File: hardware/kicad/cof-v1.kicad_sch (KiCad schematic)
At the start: 0 parts

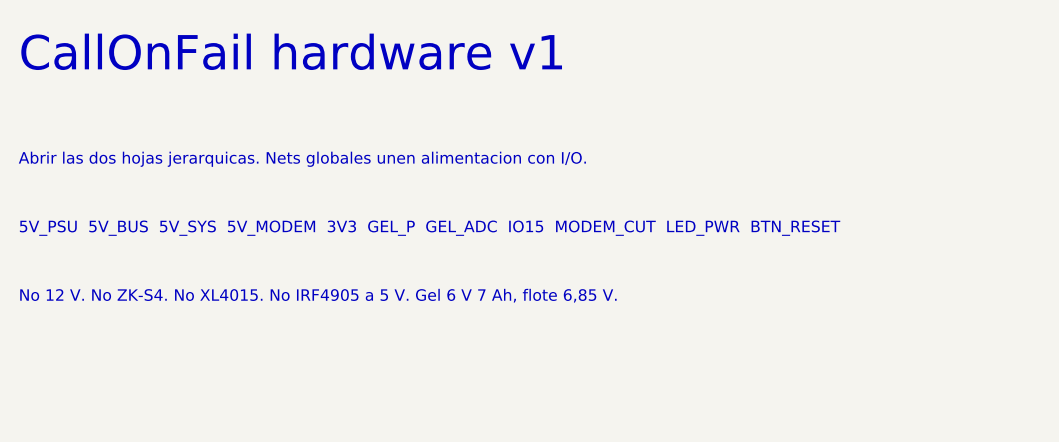
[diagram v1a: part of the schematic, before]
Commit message: Stop tracking PDFs and generated KiCad dumps; set WiFi from the web over Ethernet.
Vendor manuals, schematic PDFs, SVG previews and ERC reports do not belong in git or agent context. Firmware prefers Ethernet and accepts set_wifi/clear_wifi from the device page.

Co-authored-by: Cursor <cursoragent@cursor.com>
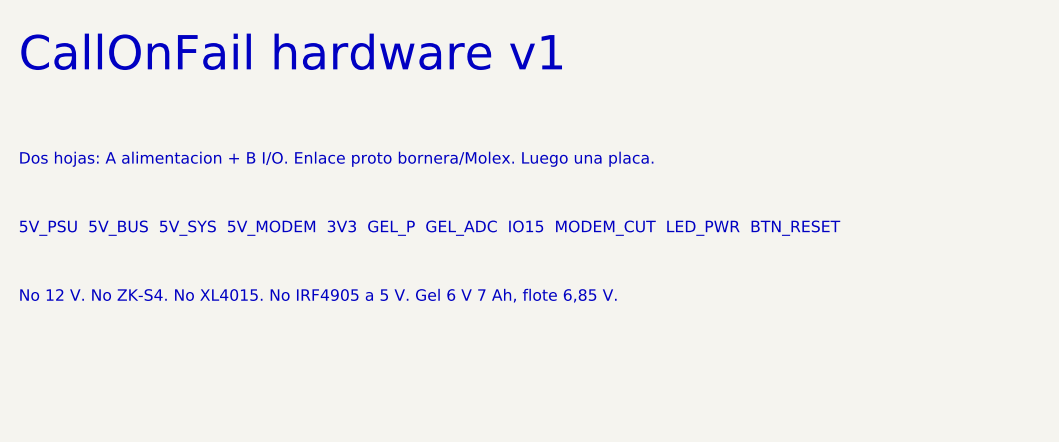
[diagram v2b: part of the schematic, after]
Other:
- note added: "Dos hojas: A alimentacion + B I/O. Enlace proto bornera/Molex. Luego una placa."
- note removed: "Abrir las dos hojas jerarquicas. Nets globales unen alimentacion con I/O."
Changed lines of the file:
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@@
 (kicad_sch
-	(version 20241209)
+	(version 20260306)
 	(generator "eeschema")
 	(generator_version "10.0")
@@
 	(title_block
 		(title "CallOnFail v1")
-		(date "2026-09-10")
-		(rev "1.2")
+		(date "2026-09-12")
+		(rev "1.4")
 		(company "CallOnFail")
 		(comment 1 "WT32-ETH01 + A7672SA-FASE + gel 6V. Ver docs/HARDWARE_V1.md")
 	)
+	(text "5V_PSU  5V_BUS  5V_SYS  5V_MODEM  3V3  GEL_P  GEL_ADC  IO15  MODEM_CUT  LED_PWR  BTN_RESET"
+		(exclude_from_sim no)
+		(at 50.8 48.26 0)
+		(effects
+			(font
+				(size 1.27 1.27)
+			)
+			(justify left bottom)
+		)
+	)
 	(text "CallOnFail hardware v1"
 		(exclude_from_sim no)
-		(at 50.80 30.48 0)
-		(effects (font (size 3.81 3.81)) (justify left bottom))
-	)
-	(text "Abrir las dos hojas jerarquicas. Nets globales unen alimentacion con I/O."
-		(exclude_from_sim no)
-		(at 50.80 40.64 0)
-		(effects (font (size 1.27 1.27)) (justify left bottom))
-	)
-	(text "5V_PSU  5V_BUS  5V_SYS  5V_MODEM  3V3  GEL_P  GEL_ADC  IO15  MODEM_CUT  LED_PWR  BTN_RESET"
-		(exclude_from_sim no)
-		(at 50.80 48.26 0)
-		(effects (font (size 1.27 1.27)) (justify left bottom))
+		(at 50.8 30.48 0)
+		(effects
+			(font
+				(size 3.81 3.81)
+			)
+			(justify left bottom)
+		)
 	)
 	(text "No 12 V. No ZK-S4. No XL4015. No IRF4905 a 5 V. Gel 6 V 7 Ah, flote 6,85 V."
 		(exclude_from_sim no)
-		(at 50.80 55.88 0)
-		(effects (font (size 1.27 1.27)) (justify left bottom))
+		(at 50.8 55.88 0)
+		(effects
+			(font
+				(size 1.27 1.27)
+			)
+			(justify left bottom)
+		)
+	)
+	(text "Dos hojas: A alimentacion + B I/O. Enlace proto bornera/Molex. Luego una placa."
+		(exclude_from_sim no)
+		(at 50.8 40.64 0)
+		(effects
+			(font
+				(size 1.27 1.27)
+			)
+			(justify left bottom)
+		)
 	)
 	(sheet
-		(at 50.80 76.20)
+		(at 50.8 76.2)
 		(size 71.12 40.64)
 		(exclude_from_sim no)
@@
 		(on_board yes)
 		(dnp no)
-		(stroke (width 0.1524) (type solid))
-		(fill (color 0 0 0 0.0000))
+		(stroke
+			(width 0.1524)
+			(type solid)
+		)
+		(fill
+			(color 0 0 0 0)
+		)
 		(property "Sheetname" "Alimentacion"
-			(at 50.80 75.00 0)
-			(effects (font (size 1.27 1.27)) (justify left bottom))
+			(at 50.8 75 0)
+			(show_name no)
+			(do_not_autoplace no)
+			(effects
+				(font
+					(size 1.27 1.27)
+				)
+				(justify left bottom)
+			)
 		)
 		(property "Sheetfile" "01-alimentacion.kicad_sch"
-			(at 50.80 117.50 0)
-			(effects (font (size 1.27 1.27)) (justify left top))
+			(at 50.8 117.5 0)
+			(show_name no)
+			(do_not_autoplace no)
+			(effects
+				(font
+					(size 1.27 1.27)
+				)
+				(justify left top)
+			)
 		)
 	)
 	(sheet
-		(at 160.02 76.20)
+		(at 160.02 76.2)
 		(size 81.28 40.64)
 		(exclude_from_sim no)
@@
 		(on_board yes)
 		(dnp no)
-		(stroke (width 0.1524) (type solid))
-		(fill (color 0 0 0 0.0000))
+		(stroke
+			(width 0.1524)
+			(type solid)
+		)
+		(fill
+			(color 0 0 0 0)
+		)
 		(property "Sheetname" "ESP32 modem sensores"
-			(at 160.02 75.00 0)
-			(effects (font (size 1.27 1.27)) (justify left bottom))
+			(at 160.02 75 0)
+			(show_name no)
+			(do_not_autoplace no)
+			(effects
+				(font
+					(size 1.27 1.27)
+				)
+				(justify left bottom)
+			)
 		)
 		(property "Sheetfile" "02-io.kicad_sch"
-			(at 160.02 117.50 0)
-			(effects (font (size 1.27 1.27)) (justify left top))
+			(at 160.02 117.5 0)
+			(show_name no)
+			(do_not_autoplace no)
+			(effects
+				(font
+					(size 1.27 1.27)
+				)
+				(justify left top)
+			)
 		)
 	)
@@
 		)
 	)
-	(embedded_fonts no)
 )
